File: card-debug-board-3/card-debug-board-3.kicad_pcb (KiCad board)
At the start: 4 copper layers, 47 x 63.5 mm, 87 parts, among them J1 USB4105-GF-A, J2 USB4105-GF-A, J3 Conn_01x05, J4 5040501291, J5 2-1734592-0, Q1 PMV450ENEAR, SW1 B3F-1000, SW2 PCM13SMTR, SW3 B3F-1000, SW4 78RB02T, U1 MIC5205-3.3YM5, U2 W25Q16JVSS, U3 RP2040, U4 74AUP1G17, U5 74AUP1G17, U6 IP4234CZ6,125, U7 IP4234CZ6,125, Y1 12 MHz

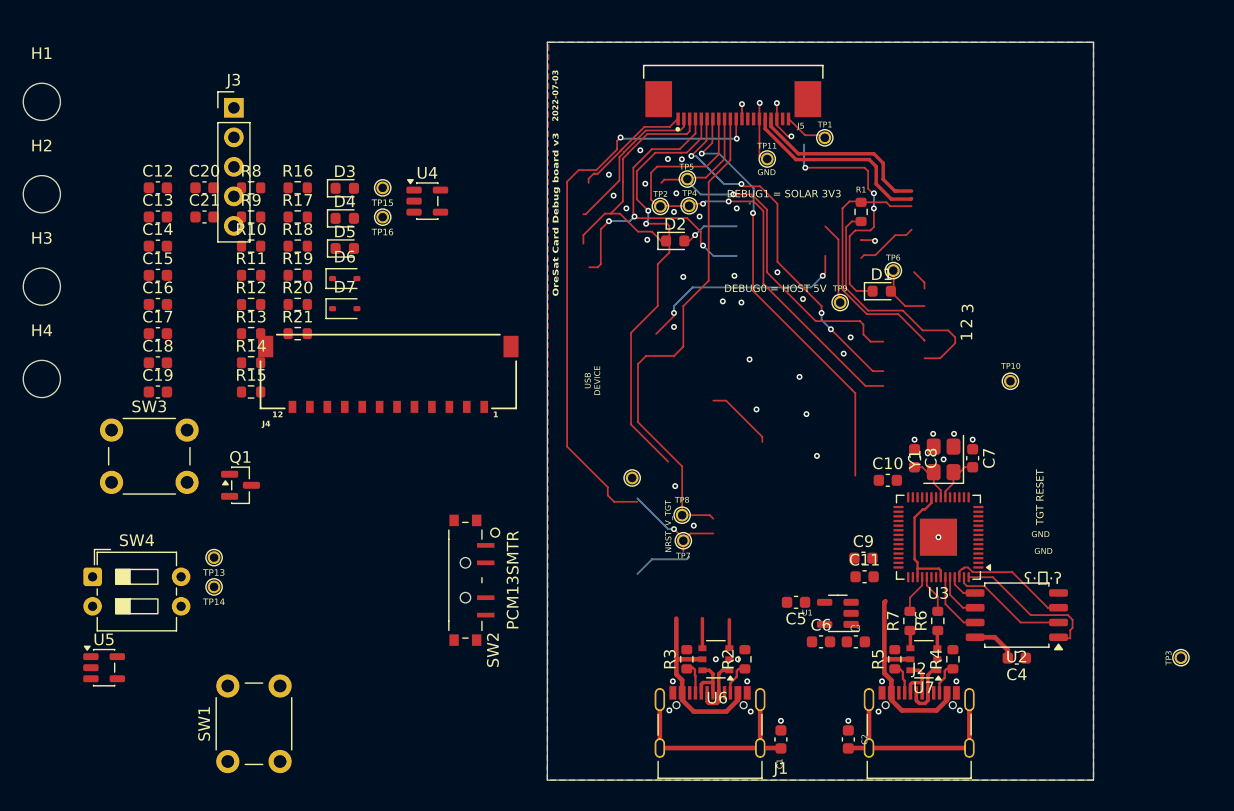
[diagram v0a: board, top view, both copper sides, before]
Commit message: More layout.
Also added 1k resistor to crystal, starting to move things around for final layout.
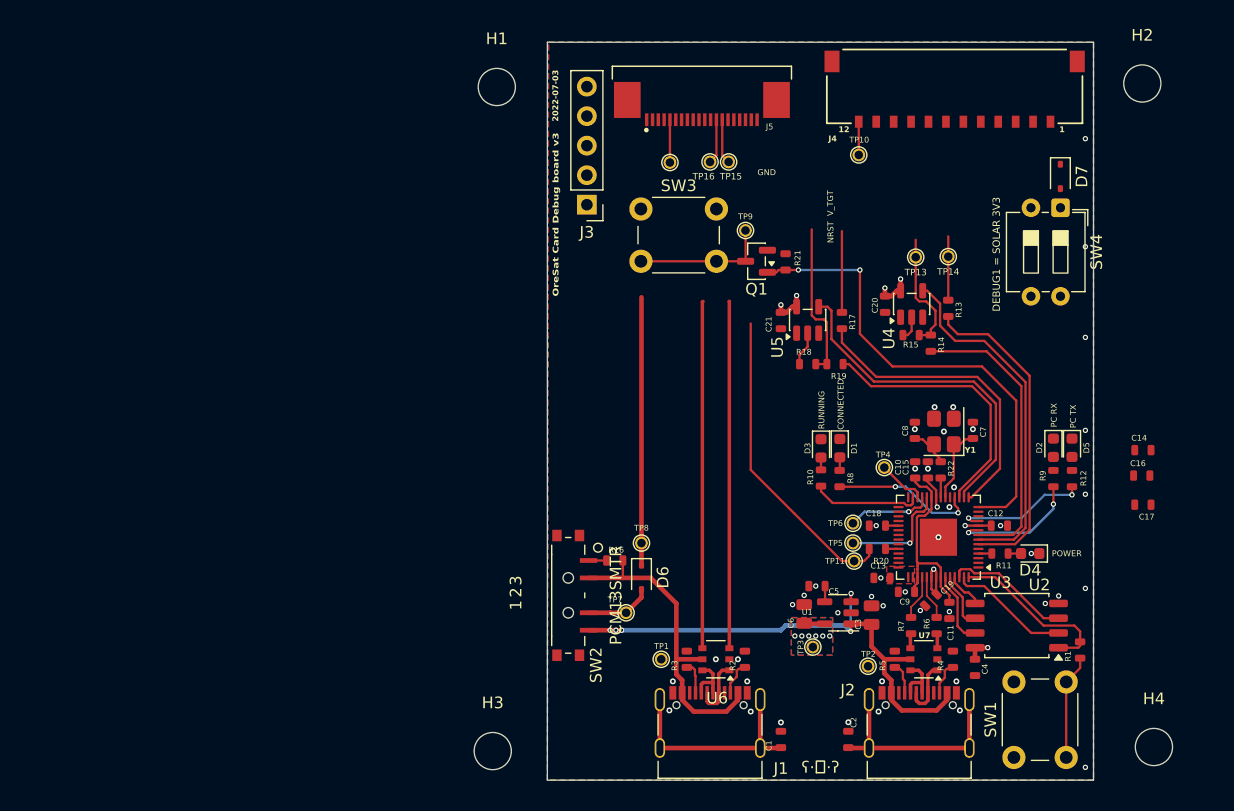
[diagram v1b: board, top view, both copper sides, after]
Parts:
- added R22: 1k, oresat-passives:0603-C-NOSILK, F.Cu at (176.8, 83.3)
- C1, C10, C11, C12, C13, C14, C15, C16, C17, C18, C19, C2, C20, C21, C4, C5, C7, C8, C9: footprint Capacitor_SMD:C_0603_1608Metric -> oresat-passives:0603-C-NOSILK
- C3, C6: footprint Capacitor_SMD:C_0603_1608Metric -> oresat-passives:0805-C-NOSILK
- R1, R10, R11, R12, R13, R14, R15, R16, R17, R18, R19, R2, R20, R21, R3, R4, R5, R6, R7, R8, R9: footprint Resistor_SMD:R_0603_1608Metric -> oresat-passives:0603-C-NOSILK
- moved H4 100.8 mm to (195.2, 107.2)
- moved H2 95.2 mm to (194.2, 50.0)
- moved SW4 89.1 mm to (187.2, 60.7), turned to -90 degrees
- moved C14 86.6 mm to (194.2, 81.6)
- moved C17 86.0 mm to (194.2, 86.3), turned to 180 degrees
- moved C16 85.9 mm to (194.2, 83.8)
- moved C12 78.0 mm to (181.9, 88.1)
- moved R9 72.6 mm to (186.6, 84.0), turned to -90 degrees
- moved R12 72.2 mm to (188.2, 84.0), turned to -90 degrees
- moved C13 69.6 mm to (171.8, 92.6)
- moved TP14 69.3 mm to (177.5, 65.0)
- moved C19 68.9 mm to (176.0, 94.5), turned to 45 degrees
- moved R11 68.7 mm to (181.9, 90.5), turned to 180 degrees
- moved C15 68.3 mm to (175.8, 83.3), turned to -90 degrees
- moved SW1 67.7 mm to (183.2, 108.0)
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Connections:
- C8 pad 2: Net-(U3-XOUT) -> Net-(C8-Pad2)
- Y1 pad 4: Net-(U3-XOUT) -> Net-(C8-Pad2)
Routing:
- net (no net): track 97.5 -> 0.00 mm, vias 2 -> 0
- net GND: track 88.2 -> 0.00 mm, vias 56 -> 44
- net /NRESET: track 56.7 -> 11.7 mm, vias 2 -> 0
- net /RESET_TARGET: track 0.00 -> 41.3 mm, vias 0 -> 2
- net /DEBUG0/5VUSBHOST: track 30.3 -> 0.00 mm, vias 3 -> 0
- net /UART1_RX: track 0.00 -> 30.2 mm
- net /SWDIO/UART0RX: track 0.00 -> 29.3 mm
- net /UART1_TX: track 0.00 -> 27.7 mm
- net /SWDCLK/UART0TX: track 0.00 -> 26.5 mm
- net Net-(U3-GPIO6): track 0.00 -> 25.1 mm
- net /SWDCLK: track 31.6 -> 7.00 mm, vias 4 -> 0
- net /SWDIO: track 37.5 -> 13.5 mm, vias 2 -> 0
- net Net-(U3-GPIO14): track 0.00 -> 23.2 mm
- net /VTARGET: track 5.53 -> 26.8 mm
- net VBUS2: track 24.9 -> 46.0 mm, vias 0 -> 5
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- added copper zone on B.Cu, net +3.3V
- added copper zone on F.Cu, net +3.3V
- added copper zone on In2.Cu, net +3.3V
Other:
- board text added: "CONNECTED"
- board text added: "PC RX"
- board text added: "PC TX"
- board text added: "POWER"
- board text added: "RUNNING"
- board text removed: "DEBUG0 = HOST 5V"
- board text removed: "TGT RESET"
- board text removed: "USB DEVICE"

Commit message: Initial Card Debug Board v3
Cleaned up routing, added test points that Pete suggested, routed as best and as quickly as possible!
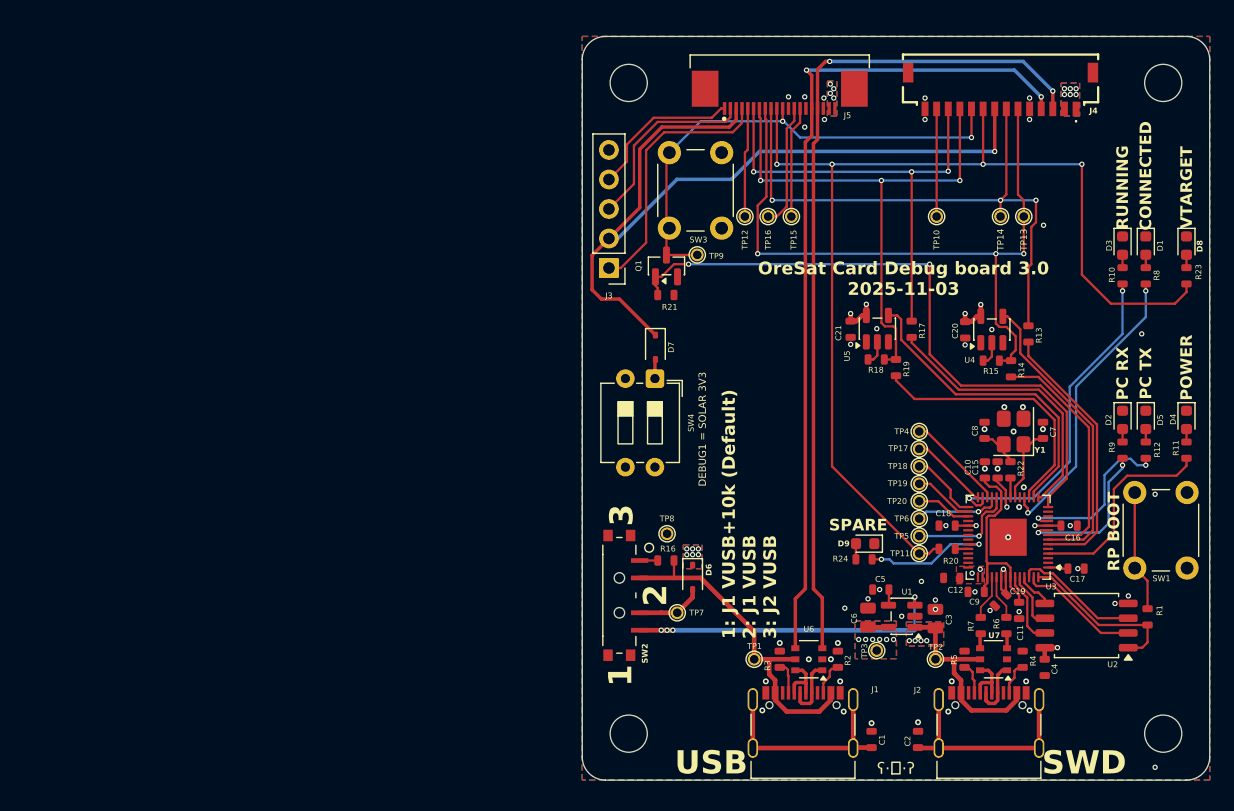
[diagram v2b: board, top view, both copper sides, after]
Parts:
- removed C13, C14: 2.2u, oresat-passives:0603-C-NOSILK
- added D8: GRN, LED_SMD:LED_0603_1608Metric, F.Cu at (198.0, 64.0)
- added D9: AMB, LED_SMD:LED_0603_1608Metric, F.Cu at (170.3, 89.7)
- added R23: 1k, oresat-passives:0603-C-NOSILK, F.Cu at (198.0, 66.6)
- added R24: 1k, oresat-passives:0603-C-NOSILK, F.Cu at (170.2, 91.0)
- added TP17: TestPoint-MinTH, oresat-misc:TestPoint-MinTH, F.Cu at (175.0, 81.5)
- added TP18: TestPoint-MinTH, oresat-misc:TestPoint-MinTH, F.Cu at (175.0, 83.0)
- added TP19: TestPoint-MinTH, oresat-misc:TestPoint-MinTH, F.Cu at (175.0, 84.5)
- added TP20: TestPoint-MinTH, oresat-misc:TestPoint-MinTH, F.Cu at (175.0, 86.0)
- J4: footprint oresat-connectors:J-MOLEX-5040501291 -> oresat-connectors:J-JST-SM14BSHLSTF
- moved SW4 37.9 mm to (152.3, 75.4)
- moved D7 37.8 mm to (152.3, 72.8)
- moved R8 31.6 mm to (194.5, 66.6)
- moved D1 31.6 mm to (194.5, 64.0)
- moved D3 31.3 mm to (192.5, 64.0)
- moved R10 31.2 mm to (192.5, 66.6)
- moved SW1 27.2 mm to (198.1, 85.2), turned to -90 degrees
- moved R11 18.4 mm to (198.0, 81.6), turned to -90 degrees
- moved D4 17.7 mm to (198.0, 79.0), turned to -90 degrees
- moved H3 11.8 mm to (150.0, 106.0)
- moved H1 11.4 mm to (150.0, 50.0)
- moved R21 10.7 mm to (153.2, 68.2), turned to 180 degrees
- moved TP13 9.94 mm to (184.0, 61.5)
- moved TP10 8.54 mm to (176.5, 61.5)
- moved SW3 8.47 mm to (158.0, 56.0), turned to -90 degrees
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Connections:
- J4 pad 10: /SWDIO -> /NRESET
- J4 pad 11: /SWDCLK -> /SWDIO
- J4 pad 12: Net-(J4-SWO) -> /SWDCLK
- J4 pad 13: GND -> Net-(J4-SWO)
- J4 pad 2: /CARD_USB_DP -> /VBUSP
- J4 pad 3: /CARD_USB_DM -> /CARD_USB_DP
- J4 pad 4: GND -> /CARD_USB_DM
- J4 pad 5: /CARD_TX -> GND
- J4 pad 6: /CARD_RX -> /CARD_TX
- J4 pad 7: /DBG1/SM3V3 -> /CARD_RX
- J4 pad 8: /VTARGET -> /DBG1/SM3V3
- J4 pad 9: /NRESET -> /VTARGET
- U3 pad 28: unconnected-(U3-GPIO17-Pad28) -> Net-(U3-GPIO17)
- U3 pad 29: unconnected-(U3-GPIO18-Pad29) -> Net-(U3-GPIO18)
- U3 pad 30: unconnected-(U3-GPIO19-Pad30) -> Net-(U3-GPIO19)
- U3 pad 31: unconnected-(U3-GPIO20-Pad31) -> Net-(U3-GPIO20)
- U3 pad 37: unconnected-(U3-GPIO25-Pad37) -> Net-(U3-GPIO25)
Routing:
- net /DBG1/SM3V3: track 0.00 -> 71.2 mm, vias 0 -> 1
- net /VTARGET: track 26.8 -> 94.9 mm, vias 0 -> 4
- net /CARD_TX: track 10.4 -> 59.8 mm, vias 0 -> 3
- net /CARD_RX: track 5.50 -> 51.2 mm, vias 0 -> 3
- net /CARD_USB_DP: track 29.9 -> 73.4 mm, vias 0 -> 2
- net /CARD_USB_DM: track 29.9 -> 72.7 mm, vias 0 -> 2
- net /SWDCLK: track 7.00 -> 40.4 mm, vias 0 -> 3
- net /SWDIO: track 13.5 -> 46.9 mm, vias 0 -> 3
- net /NRESET: track 11.7 -> 42.9 mm, vias 0 -> 2
- net /VBUSP: track 23.0 -> 0.00 mm, vias 0 -> 16
- net /DEBUG0/5VUSBHOST: track 0.00 -> 22.5 mm
- net /DAP_TARGET_RUNNING_LED: track 9.45 -> 29.1 mm, vias 0 -> 2
- net /POWER_LED: track 1.16 -> 17.9 mm
- net /DEBUG2: track 0.00 -> 16.4 mm
- net /RESET_TARGET: track 41.3 -> 56.2 mm
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- added copper zone on B.Cu, net /VBUSP
- added copper zone on F.Cu, net /VBUSP
- added copper zone on In2.Cu, net /VBUSP
- added copper zone on B.Cu, net VBUS2
- added copper zone on F.Cu, net VBUS2
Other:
- board size 47 x 63.5 mm -> 54 x 64 mm
- board text added: "1: J1 VUSB+10k (Default) 2: J1 VUSB 3: J2 VUSB"
- board text added: "OreSat Card Debug board ${REVISION} ${ISSUE_DATE}"
- board text added: "RP BOOT"
- board text added: "SPARE"
- board text added: "SWD"
- board text added: "USB"
- board text added: "VTARGET"
- board text removed: "1: VUSB through 10k for Octavo USB 2: VUSB straight to power Octavo 3: STLINK VUSB to VBUSP"
- board text removed: "2022-07-03"
- board text removed: "GND"
- board text removed: "NRST"
- board text removed: "OreSat Card Debug board v3"
- board text removed: "V_TGT"

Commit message: Final polish for manufacturing or v3.
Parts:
- moved TP4 1.50 mm to (175.0, 78.5)
- moved TP17 1.25 mm to (175.0, 80.2)
- moved TP18 1.00 mm to (175.0, 82.0)
- moved TP19 0.75 mm to (175.0, 83.8)
- moved TP11 0.50 mm to (175.0, 91.0)
- moved TP20 0.50 mm to (175.0, 85.5)
- moved TP5 0.25 mm to (175.0, 89.2)
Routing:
- net Net-(U3-RUN): track 8.46 -> 9.73 mm
- net /VTARGET: track 94.9 -> 96.1 mm
- net Net-(U3-GPIO17): track 6.78 -> 7.62 mm
- net /NRESET: track 42.9 -> 43.6 mm
- net Net-(U3-GPIO18): track 6.08 -> 6.67 mm
- net GND: vias 56 -> 153
- net /DAP_CONNECTED_LED: vias 2 -> 3
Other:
- board text added: "OFF ON"

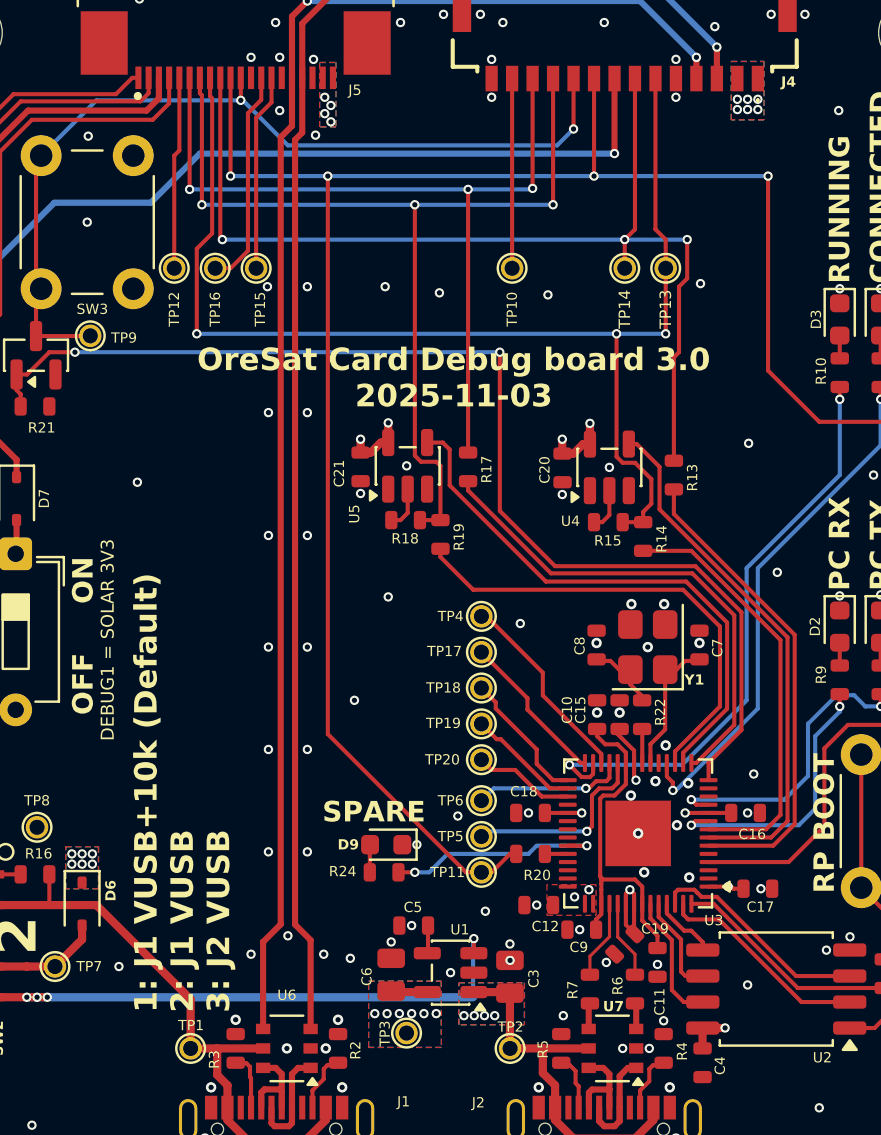
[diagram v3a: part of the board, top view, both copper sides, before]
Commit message: Small fix to create v3.1 (functionally the same as v3.0), updated BOM, and added a README.
The BOM is now officially finished and can be used to order parts. The README now points the Google Doc design notes. Updated the board and schematic to v3.1 just because we found a small error in v3.0 that we should fix ASAP.
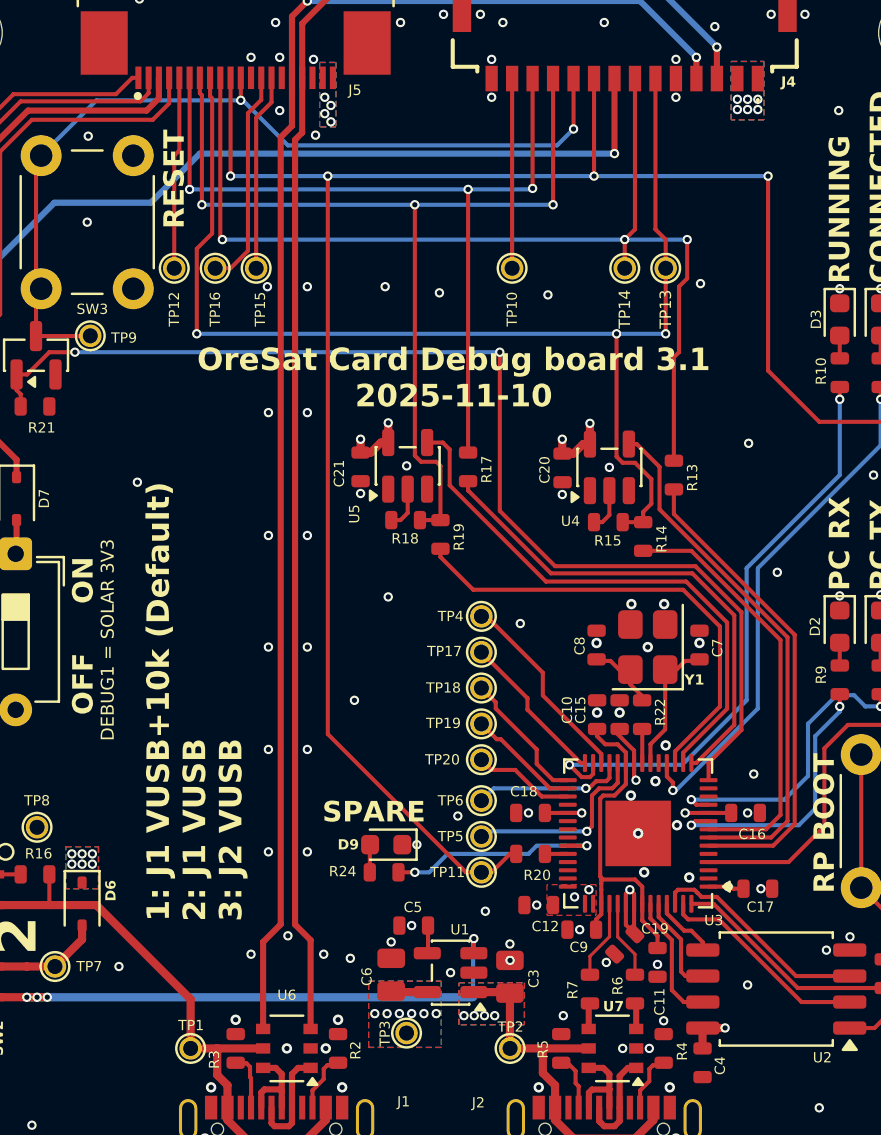
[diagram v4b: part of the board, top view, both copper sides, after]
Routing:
- net /DAP_CONNECTED_LED: vias 3 -> 2
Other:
- board text added: "RESET"
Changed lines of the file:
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@@
 	(title_block
 		(title "Card Debug Board")
-		(date "2025-11-03")
-		(rev "3.0")
+		(date "2025-11-10")
+		(rev "3.1")
 		(company "Portland State Aerosapce Society")
 	)
@@
 			)
 			(rotate
+				(xyz -0 -0 -0)
+			)
+		)
+		(model "${ORESAT_LIBRARIES}/oresat-3dmodels/SM14B-SHLS-TF.stp"
+			(offset
 				(xyz 0 0 0)
 			)
+			(scale
+				(xyz 1 1 1)
+			)
+			(rotate
+				(xyz -0 -0 -0)
+			)
 		)
 	)
@@
 		)
 		(embedded_fonts no)
-		(model "${KICAD9_3DMODEL_DIR}/Connector_USB.3dshapes/USB_C_Receptacle_Palconn_UTC16-G.step"
+		(model "${KICAD9_3DMODEL_DIR}/Connector_USB.3dshapes/USB_C_Receptacle_GCT_USB4105-xx-A_16P_TopMnt_Horizontal.step"
 			(offset
-				(xyz 0 0 0)
+				(xyz 0 -1.5 -0.1)
 			)
 			(scale
@@
 			)
 			(rotate
-				(xyz 0 0 0)
+				(xyz -0 -0 -0)
 			)
 		)
@@
 		)
 		(embedded_fonts no)
-		(model "${KICAD9_3DMODEL_DIR}/Connector_USB.3dshapes/USB_C_Receptacle_Palconn_UTC16-G.step"
+		(model "${KICAD9_3DMODEL_DIR}/Connector_USB.3dshapes/USB_C_Receptacle_GCT_USB4105-xx-A_16P_TopMnt_Horizontal.step"
 			(offset
-				(xyz 0 0 0)
+				(xyz 0 -1.25 -0.05)
 			)
 			(scale
@@
 			)
 			(rotate
-				(xyz 0 0 0)
+				(xyz -0 -0 -0)
 			)
 		)
@@
 	)
 	(gr_text "1: J1 VUSB+10k (Default)\n2: J1 VUSB\n3: J2 VUSB"
-		(at 160.4 97.85 90)
+		(at 161 93.4 90)
 		(layer "F.SilkS")
 		(effects
@@
 		)
 	)
+	(gr_text "RESET"
+		(at 160 57.15 90)
+		(layer "F.SilkS")
+		(effects
+			(font
+				(size 1 1)
+				(thickness 0.2)
+				(bold yes)
+			)
+		)
+	)
 	(gr_text "RUNNING"
 		(at 192.5 62.25 90)
@@
 		(drill 0.254)
 		(layers "F.Cu" "B.Cu")
-		(net 28)
-	)
-	(via
-		(at 185.1 86.65)
-		(size 0.508)
-		(drill 0.254)
-		(layers "F.Cu" "B.Cu")
